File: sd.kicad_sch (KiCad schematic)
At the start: 7 parts, among them J5 SD_Card_Receptacle

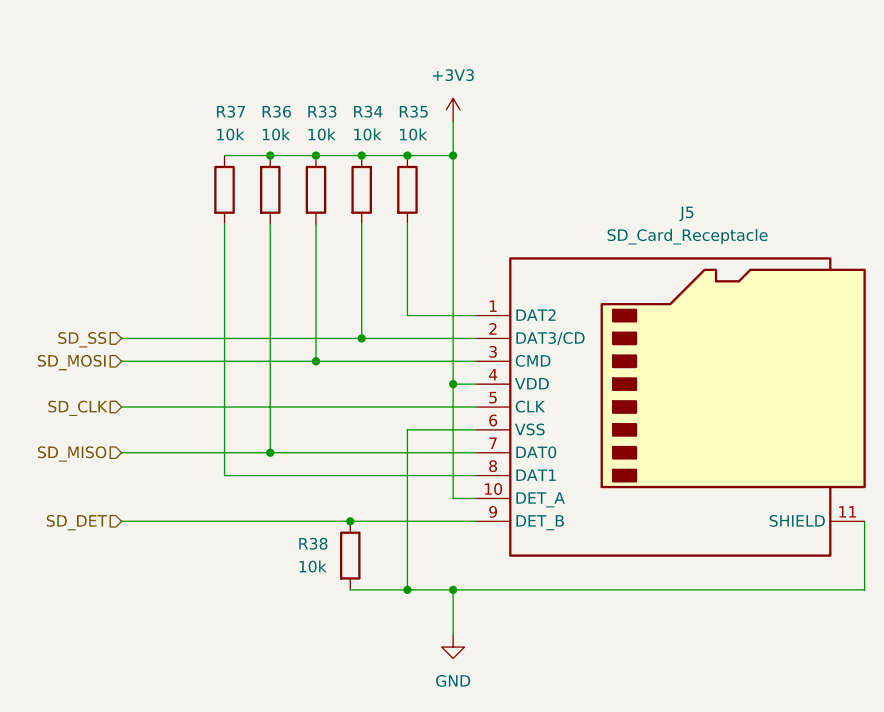
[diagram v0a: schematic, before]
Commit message: fix usb and add esd diodes, some other checks
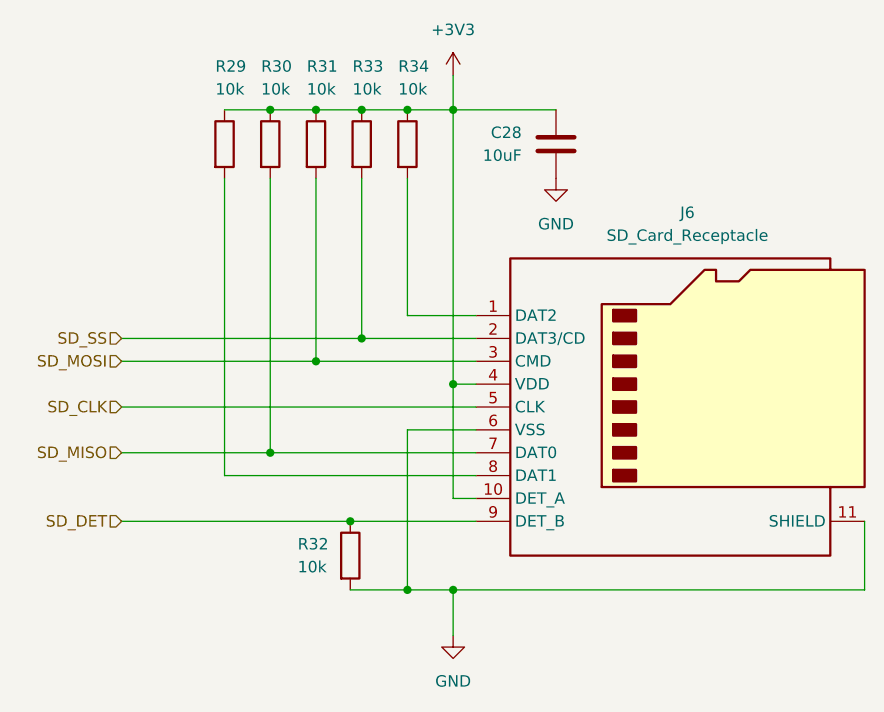
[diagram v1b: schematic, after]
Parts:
- added C28: 10uF, Capacitor_SMD:C_0603_1608Metric, symbol Device:C
- renumbered J5 to J6, R37 to R29, R36 to R30, R33 to R31, R38 to R32, R34 to R33, R35 to R34
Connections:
- net +3V3: now also C28.1
- net GND: now also C28.2
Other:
- moved on the sheet: R29, R30, R31, R33, R34

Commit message: add silkscreen, optimize layout and replace sd card peripheral
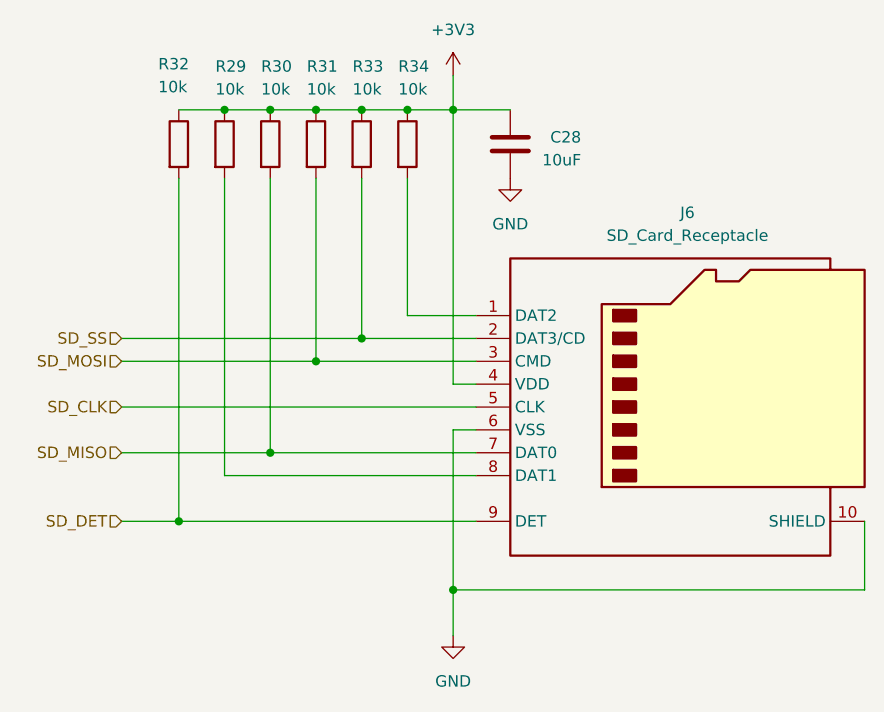
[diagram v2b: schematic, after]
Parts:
- J6: footprint Connector_Card:microSD_HC_Molex_104031-0811 -> RP2350_60QFN_minimal:SHOU HAN; symbol Connector:Micro_SD_Card_Det2 -> Connector:Micro_SD_Card_Det1; LCSC C585350 -> C393941; Manufacturer MOLEX -> SHOU HAN; Manufacturer Part Number 1040310811 -> TF PUSH
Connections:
- net +3V3: now also R32.1; no longer J6.10 (DET_A)
- net GND: now also J6.10 (SHIELD); no longer J6.11 (SHIELD), R32.2
- net SD_DET: now also R32.2; no longer R32.1
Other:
- moved on the sheet: C28, R32

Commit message: align some components with inventory
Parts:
- C28: footprint Capacitor_SMD:C_0603_1608Metric -> Capacitor_SMD:C_0805_2012Metric
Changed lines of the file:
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@@
 			)
 		)
-		(property "Footprint" "Capacitor_SMD:C_0603_1608Metric"
+		(property "Footprint" "Capacitor_SMD:C_0805_2012Metric"
 			(at 148.8948 62.23 0)
 			(effects
